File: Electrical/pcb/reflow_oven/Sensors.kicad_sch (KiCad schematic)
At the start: 97 parts, among them J10 THC IN, J11 THC IN, J12 NTC_A IN, J13 NTC_B IN, J6 Line IN, J7 Heater_A, J8 Line IN, J9 Heater_B, T1 ZMPT101B, T2 ZMPT101B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

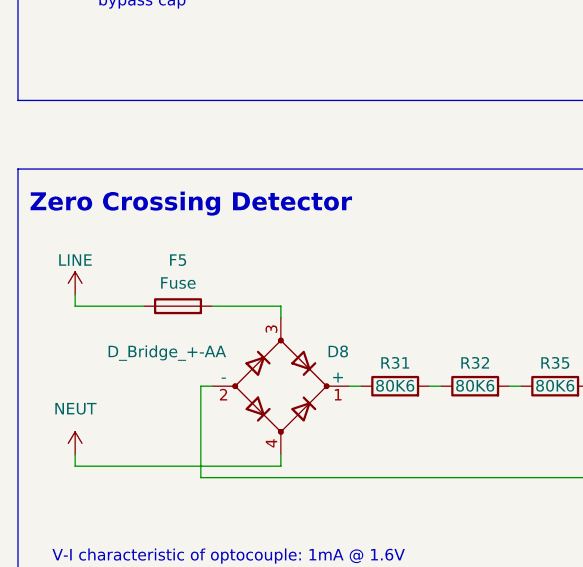
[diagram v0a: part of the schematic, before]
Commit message: addon
documentation pics
adjust oshw logo
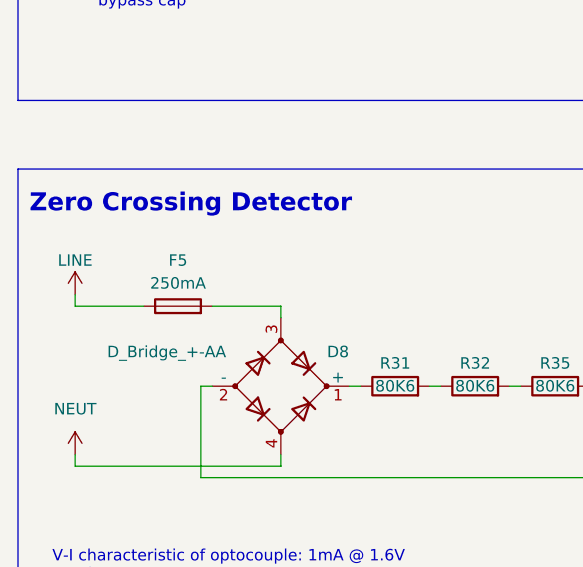
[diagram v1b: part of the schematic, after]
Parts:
- F5: value Fuse -> 250mA
- TP1, TP12, TP13, TP14, TP15, TP16, TP17, TP18, TP19, TP2: now left out of the parts list
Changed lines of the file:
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@@
   )
   (symbol (lib_id "Connector:TestPoint") (at 114.3 33.02 0) (unit 1)
-    (in_bom yes) (on_board yes)
+    (in_bom no) (on_board yes)
     (property "Reference" "TP1" (id 0) (at 113.03 27.94 0)
       (effects (font (size 1.27 1.27)) (justify left))
@@
   )
   (symbol (lib_id "Connector:TestPoint") (at 223.52 106.68 0) (unit 1)
-    (in_bom yes) (on_board yes)
+    (in_bom no) (on_board yes)
     (property "Reference" "TP19" (id 0) (at 222.25 101.6 0)
       (effects (font (size 1.27 1.27)) (justify left))
@@
   )
   (symbol (lib_id "Connector:TestPoint") (at 180.34 57.15 0) (unit 1)
-    (in_bom yes) (on_board yes)
+    (in_bom no) (on_board yes)
     (property "Reference" "TP15" (id 0) (at 179.07 52.07 0)
       (effects (font (size 1.27 1.27)) (justify left))
@@
   )
   (symbol (lib_id "Connector:TestPoint") (at 92.71 175.26 0) (unit 1)
-    (in_bom yes) (on_board yes)
+    (in_bom no) (on_board yes)
     (property "Reference" "TP12" (id 0) (at 91.44 170.18 0)
       (effects (font (size 1.27 1.27)) (justify left))
@@
   )
   (symbol (lib_id "Connector:TestPoint") (at 193.04 242.57 0) (unit 1)
-    (in_bom yes) (on_board yes)
+    (in_bom no) (on_board yes)
     (property "Reference" "TP17" (id 0) (at 191.77 237.49 0)
       (effects (font (size 1.27 1.27)) (justify left))
@@
   )
   (symbol (lib_id "Connector:TestPoint") (at 157.48 242.57 0) (unit 1)
-    (in_bom yes) (on_board yes)
+    (in_bom no) (on_board yes)
     (property "Reference" "TP14" (id 0) (at 156.21 237.49 0)
       (effects (font (size 1.27 1.27)) (justify left))
@@
   )
   (symbol (lib_id "Connector:TestPoint") (at 223.52 46.99 0) (unit 1)
-    (in_bom yes) (on_board yes)
+    (in_bom no) (on_board yes)
     (property "Reference" "TP18" (id 0) (at 222.25 41.91 0)
       (effects (font (size 1.27 1.27)) (justify left))
@@
     (in_bom yes) (on_board yes)
     (property "Reference" "F5" (id 0) (at 35.56 163.83 90))
-    (property "Value" "Fuse" (id 1) (at 35.56 166.37 90))
+    (property "Value" "250mA" (id 1) (at 35.56 166.37 90))
     (property "Footprint" "footprint_lib:Circular_fuse" (id 2) (at 35.56 170.688 90)
       (effects (font (size 1.27 1.27)) hide)
@@
   )
   (symbol (lib_id "Connector:TestPoint") (at 180.34 116.84 0) (unit 1)
-    (in_bom yes) (on_board yes)
+    (in_bom no) (on_board yes)
     (property "Reference" "TP16" (id 0) (at 179.07 111.76 0)
       (effects (font (size 1.27 1.27)) (justify left))
@@
   )
   (symbol (lib_id "Connector:TestPoint") (at 114.3 92.71 0) (unit 1)
-    (in_bom yes) (on_board yes)
+    (in_bom no) (on_board yes)
     (property "Reference" "TP2" (id 0) (at 113.03 87.63 0)
       (effects (font (size 1.27 1.27)) (justify left))
@@
   )
   (symbol (lib_id "Connector:TestPoint") (at 119.38 181.61 0) (unit 1)
-    (in_bom yes) (on_board yes)
+    (in_bom no) (on_board yes)
     (property "Reference" "TP13" (id 0) (at 118.11 176.53 0)
       (effects (font (size 1.27 1.27)) (justify left))

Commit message: documentazione
aggiunta documentazione
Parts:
- C26, C27, C32, C33: value 1nF -> 10nF
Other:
- note added: "V-I characteristic of optocoupler: 1mA @ 1.6V Vmain = Vrms*1.414 = 325Vac Rled = (Vmain-Vfled)/If = 323Kohm -> 4x80.6Kohm P = (If^2)*80.6Kohm = 80.6mW working voltage across resistor is ~80V"
- note removed: "V-I characteristic of optocouple: 1mA @ 1.6V Vmain = Vrms*1.414 = 325Vac Rled = (Vmain-Vfled)/If = 323Kohm -> 4x80.6Kohm P = (If^2)*80.6Kohm = 80.6mW working voltage across resistor is ~80V"
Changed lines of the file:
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@@
     (stroke (width 0) (type default) (color 0 0 0 0))
   )
-  (text "V-I characteristic of optocouple: 1mA @ 1.6V\nVmain = Vrms*1.414 = 325Vac\nRled = (Vmain-Vfled)/If = 323Kohm -> 4x80.6Kohm\nP = (If^2)*80.6Kohm = 80.6mW\nworking voltage across resistor is ~80V "
+  (text "V-I characteristic of optocoupler: 1mA @ 1.6V\nVmain = Vrms*1.414 = 325Vac\nRled = (Vmain-Vfled)/If = 323Kohm -> 4x80.6Kohm\nP = (If^2)*80.6Kohm = 80.6mW\nworking voltage across resistor is ~80V "
     (at 21.59 205.74 0)
     (effects (font (size 1.27 1.27)) (justify left bottom))
@@
       (effects (font (size 1.27 1.27)) (justify left))
     )
-    (property "Value" "1nF" (id 1) (at 207.01 59.69 90)
+    (property "Value" "10nF" (id 1) (at 207.01 59.69 90)
       (effects (font (size 1.27 1.27)) (justify left))
     )
@@
       (effects (font (size 1.27 1.27)) (justify left))
     )
-    (property "Value" "1nF" (id 1) (at 156.21 111.76 90)
+    (property "Value" "10nF" (id 1) (at 156.21 111.76 90)
       (effects (font (size 1.27 1.27)) (justify left))
     )
@@
       (effects (font (size 1.27 1.27)) (justify left))
     )
-    (property "Value" "1nF" (id 1) (at 208.28 119.38 90)
+    (property "Value" "10nF" (id 1) (at 208.28 119.38 90)
       (effects (font (size 1.27 1.27)) (justify left))
     )
@@
       (effects (font (size 1.27 1.27)) (justify left))
     )
-    (property "Value" "1nF" (id 1) (at 156.21 52.07 90)
-      (effects (font (size 1.27 1.27)) (justify left))
-    )
+    (property "Value" "10nF" (id 1) (at 156.21 52.07 90)
+      (effects (font (size 1.27 1.27)) (justify left))
+    )
